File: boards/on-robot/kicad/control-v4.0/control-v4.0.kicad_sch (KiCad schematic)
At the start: 13 parts, among them IC1 MCP23017E_SS, J1 53625-0274, J6 53625-0274, J7 53625-0274, J8 53625-0274, U1 Teensy4.1, U3 NRF24L01_Breakout

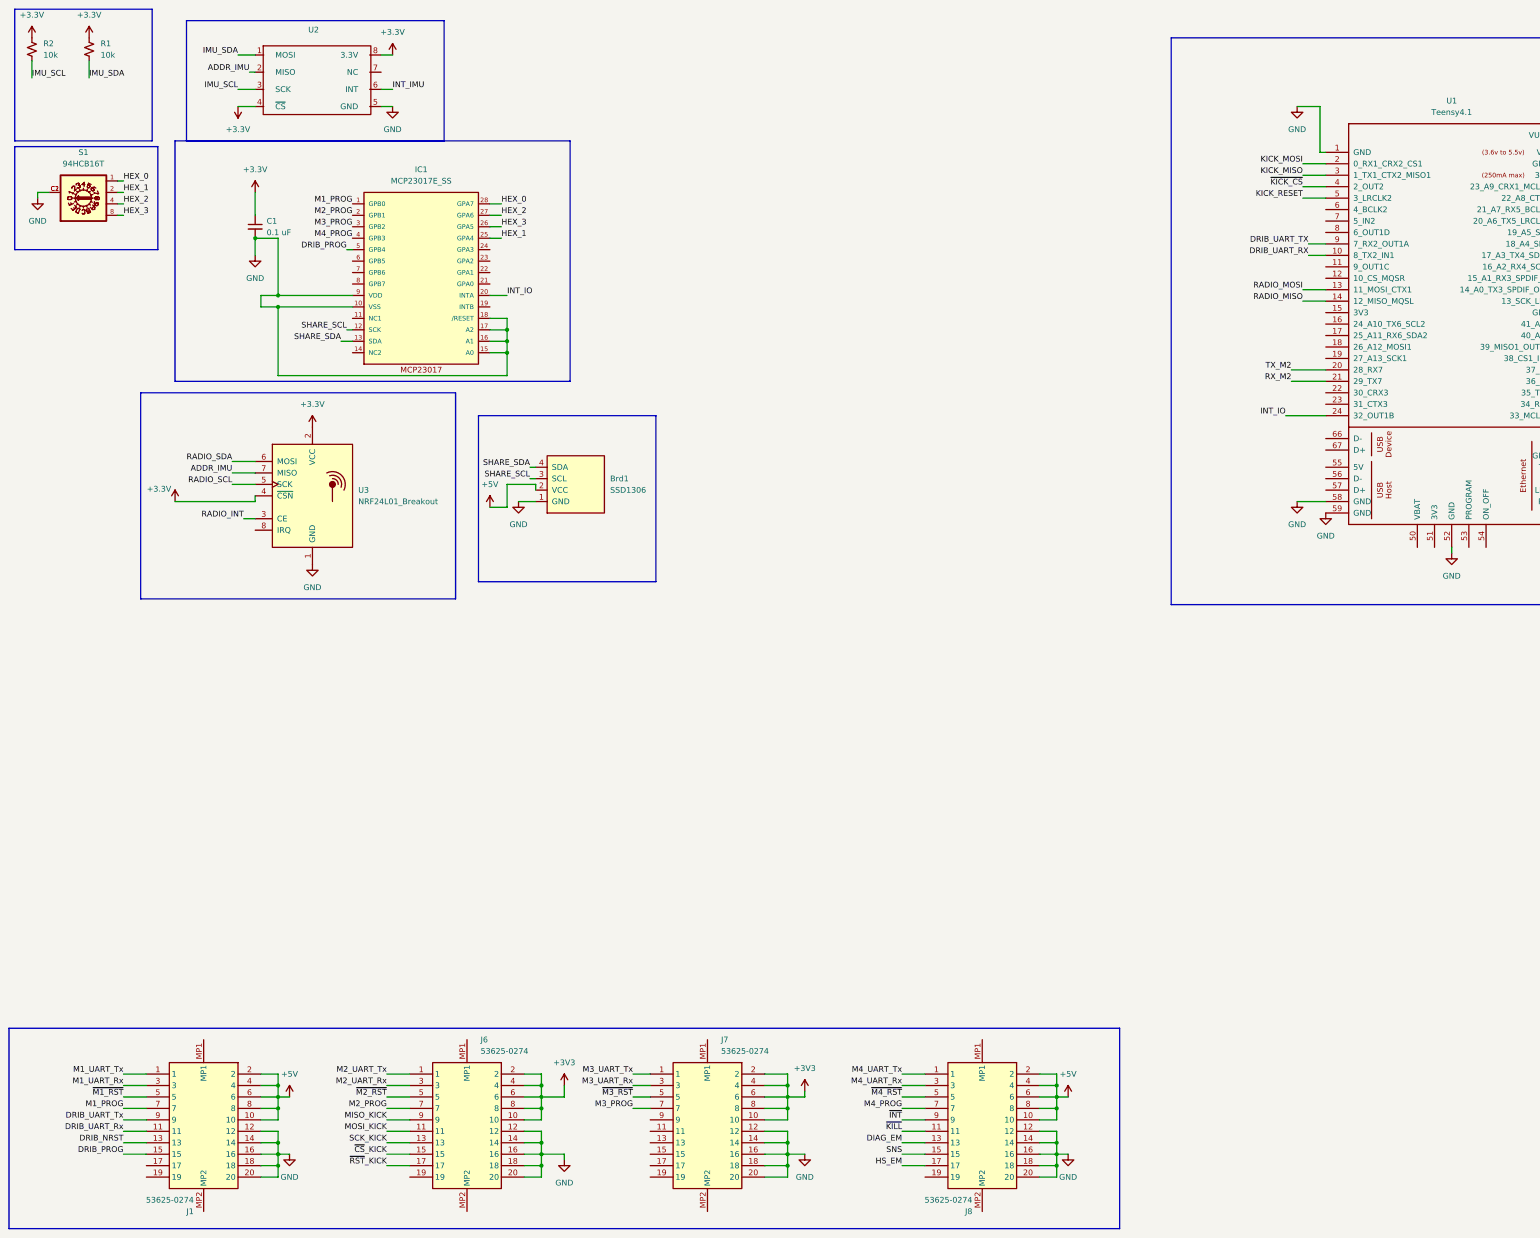
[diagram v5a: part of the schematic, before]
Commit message: migrated libraries
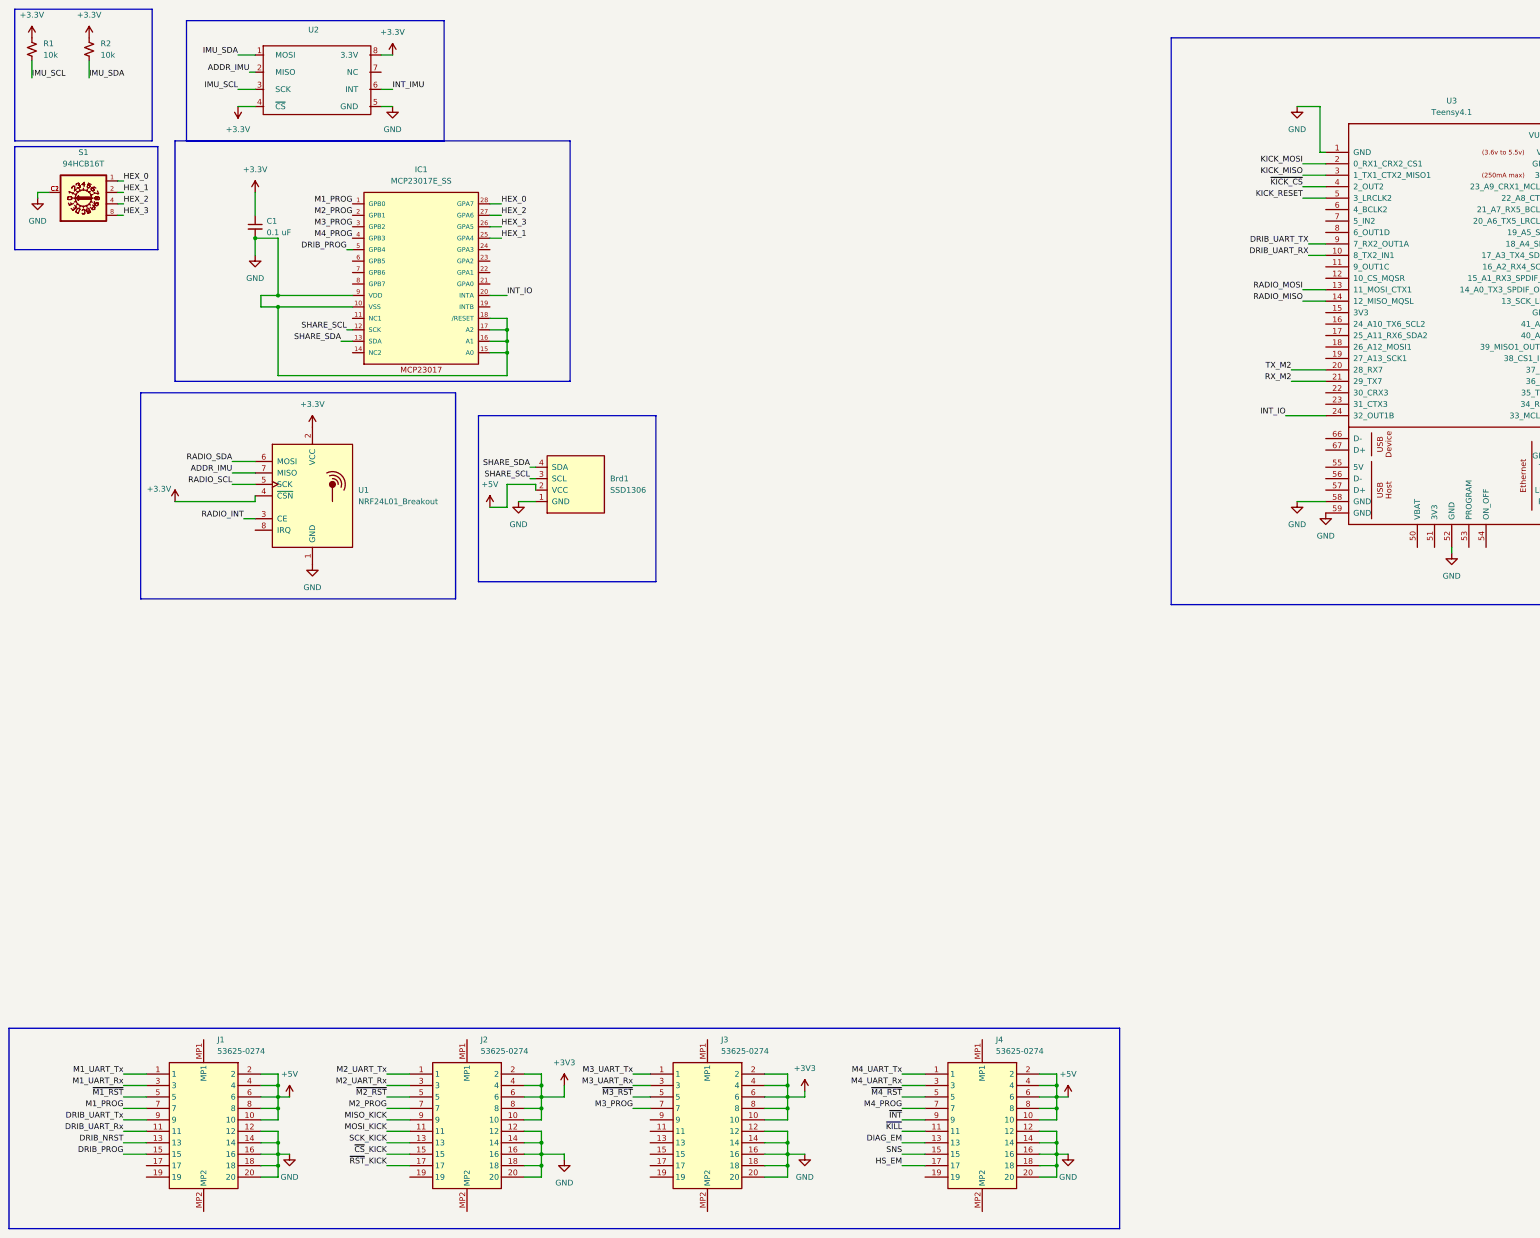
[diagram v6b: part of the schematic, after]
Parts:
- removed J6, J7, J8: 53625-0274, RoboJackets-Connectors:536250274, symbol RoboJackets-Connectors:53625-0274
- added J2, J3, J4: 53625-0274, RoboJackets-Connectors:536250274, symbol RoboJackets-Connectors:53625-0274
- U3: renamed from U1; footprint teensy.pretty-master:Teensy41 -> RoboJackets-Boards:Teensy41
- renumbered R2 to R1, R1 to R2, U3 to U1
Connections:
- net +3V3: now also J2.10, J2.2, J2.4, J2.6, J2.8, J3.10, J3.2, J3.4, J3.6, J3.8
- net +5V: now also J4.10, J4.2, J4.4, J4.6, J4.8
- net DIAG_EM: now also J4.13
- net GND: now also J2.12, J2.14, J2.16, J2.18, J2.20, J3.12, J3.14, J3.16, J3.18, J3.20, J4.12, J4.14, J4.16, J4.18, J4.20
- net HS_EM: now also J4.17
- net M2_PROG: now also J2.7
- net M2_UART_Rx: now also J2.3
- net M2_UART_Tx: now also J2.1
- net M3_PROG: now also J3.7
- net M3_UART_Rx: now also J3.3
- net M3_UART_Tx: now also J3.1
- net M4_PROG: now also J4.7
- net M4_UART_Rx: now also J4.3
- net M4_UART_Tx: now also J4.1
- net MISO_KICK: now also J2.9
- net MOSI_KICK: now also J2.11
- net SCK_KICK: now also J2.13
- net SNS: now also J4.15
- net ~{CS}_KICK: now also J2.15
- net ~{INT}: now also J4.9
- net ~{KILL}: now also J4.11
- net ~{M2_RST}: now also J2.5
- net ~{M3_RST}: now also J3.5
- net ~{M4_RST}: now also J4.5
- net ~{RST}_KICK: now also J2.17

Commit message: design review comments
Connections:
- net GND: no longer IC1.10 (VSS), IC1.15 (A0), IC1.16 (A1), IC1.17 (A2), IC1.18 (/RESET), IC1.9 (VDD)
- new net: IC1.10 (VSS), IC1.15 (A0), IC1.16 (A1), IC1.17 (A2), IC1.18 (/RESET)
- no-connect marks 0 -> 1
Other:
- note added: "CHANGE TEENSY VIN"
- note added: "We have extra pins. Remove IO expander"
- note added: "change this"
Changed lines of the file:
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@@
-	)
-	(junction
-		(at 73.66 78.74)
-		(diameter 0)
-		(color 0 0 0 0)
-	)
-	(junction
-		(at 73.66 76.2)
-		(diameter 0)
-		(color 0 0 0 0)
 	)
 	(junction
@@
 		(color 0 0 0 0)
 	)
+	(no_connect
+		(at 361.95 49.53)
+	)
 	(wire
 		(pts
@@
 	(wire
 		(pts
-			(xy 69.85 78.74) (xy 73.66 78.74)
-		)
-		(stroke
-			(width 0)
-			(type default)
-		)
-	)
-	(wire
-		(pts
 			(xy 361.95 111.76) (xy 368.3 111.76)
 		)
@@
 	(wire
 		(pts
-			(xy 73.66 76.2) (xy 90.17 76.2)
-		)
-		(stroke
-			(width 0)
-			(type default)
-		)
-	)
-	(wire
-		(pts
 			(xy 152.4 254) (xy 156.21 254)
 		)
@@
 	(wire
 		(pts
-			(xy 73.66 76.2) (xy 69.85 76.2)
-		)
-		(stroke
-			(width 0)
-			(type default)
-		)
-	)
-	(wire
-		(pts
 			(xy 246.38 266.7) (xy 248.92 266.7)
 		)
@@
 	(wire
 		(pts
-			(xy 73.66 63.5) (xy 73.66 76.2)
-		)
-		(stroke
-			(width 0)
-			(type default)
-		)
-	)
-	(wire
-		(pts
 			(xy 124.46 93.98) (xy 124.46 88.9)
 		)
@@
 		(pts
 			(xy 124.46 118.11) (xy 130.81 118.11)
-		)
-		(stroke
-			(width 0)
-			(type default)
-		)
-	)
-	(wire
-		(pts
-			(xy 69.85 76.2) (xy 69.85 78.74)
 		)
 		(stroke
@@
 		)
 	)
+	(text "CHANGE TEENSY VIN"
+		(exclude_from_sim no)
+		(at 367.284 36.576 0)
+		(effects
+			(font
+				(size 1.27 1.27)
+				(color 255 0 0 1)
+			)
+		)
+	)
+	(text "change this"
+		(exclude_from_sim no)
+		(at 22.352 63.5 0)
+		(effects
+			(font
+				(size 1.27 1.27)
+				(color 255 0 0 1)
+			)
+		)
+	)
+	(text "We have extra pins.\nRemove IO expander"
+		(exclude_from_sim no)
+		(at 293.116 84.074 0)
+		(effects
+			(font
+				(size 1.27 1.27)
+				(color 255 0 0 1)
+			)
+		)
+	)

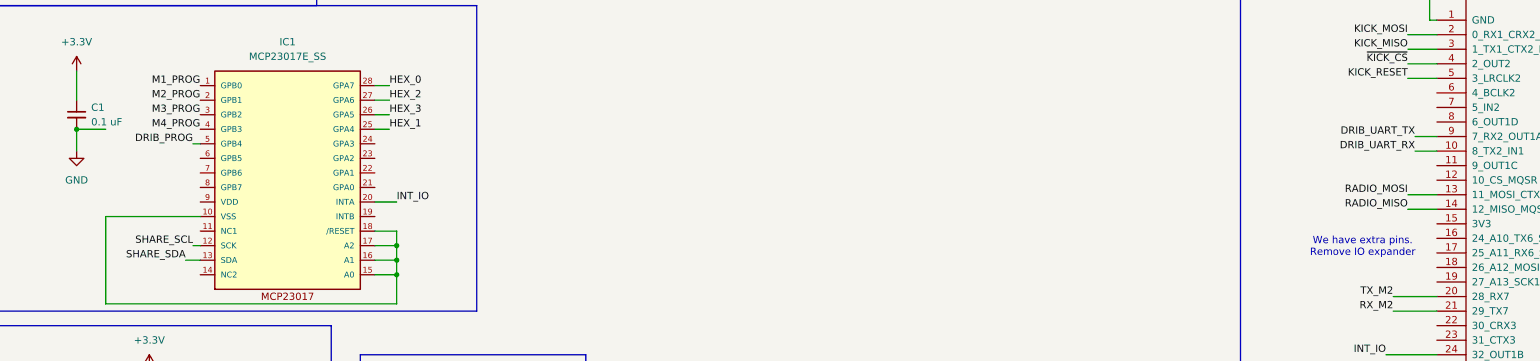
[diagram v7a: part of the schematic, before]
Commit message: fixed MCP23017E_SS wiring? (restored previous version before power label disappeared)
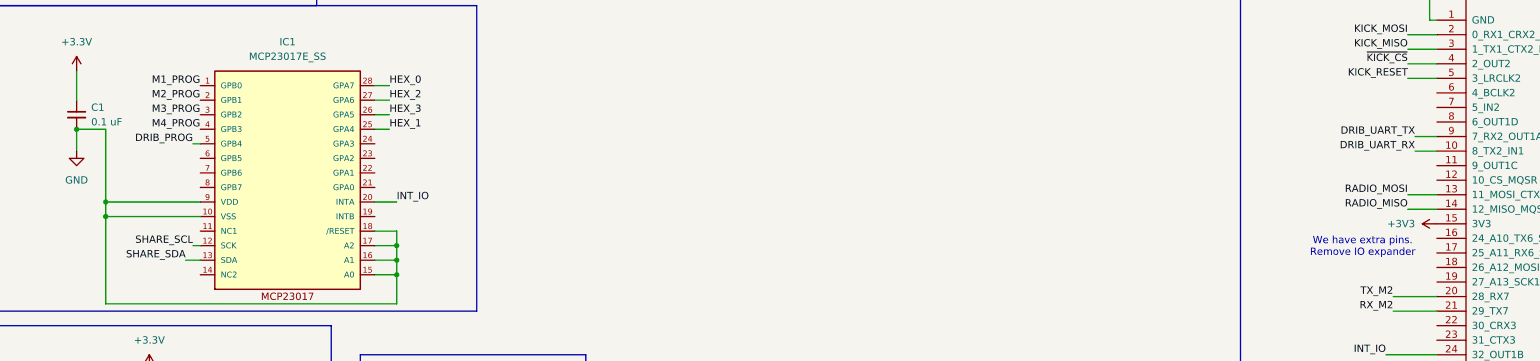
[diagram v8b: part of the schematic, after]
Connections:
- net +3V3: now also U3.15 (3V3)
- net GND: now also IC1.10 (VSS), IC1.15 (A0), IC1.16 (A1), IC1.17 (A2), IC1.18 (/RESET), IC1.9 (VDD)
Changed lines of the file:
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@@
 	)
 	(junction
+		(at 73.66 78.74)
+		(diameter 0)
+		(color 0 0 0 0)
+	)
+	(junction
 		(at 186.69 269.24)
 		(diameter 0)
@@
 		(color 0 0 0 0)
 	)
+	(junction
+		(at 73.66 76.2)
+		(diameter 0)
+		(color 0 0 0 0)
+	)
 	(no_connect
 		(at 361.95 49.53)
@@
 	(wire
 		(pts
+			(xy 73.66 76.2) (xy 90.17 76.2)
+		)
+		(stroke
+			(width 0)
+			(type default)
+		)
+	)
+	(wire
+		(pts
 			(xy 300.99 46.99) (xy 306.07 46.99)
 		)
@@
 	(wire
 		(pts
+			(xy 73.66 76.2) (xy 73.66 78.74)
+		)
+		(stroke
+			(width 0)
+			(type default)
+		)
+	)
+	(wire
+		(pts
 			(xy 132.08 254) (xy 137.16 254)
 		)
@@
 	(wire
 		(pts
+			(xy 73.66 63.5) (xy 73.66 76.2)
+		)
+		(stroke
+			(width 0)
+			(type default)
+		)
+	)
+	(wire
+		(pts
 			(xy 128.27 256.54) (xy 132.08 256.54)
 		)
@@
 		(on_board yes)
 		(dnp no)
-		(fields_autoplaced yes)
 		(property "Reference" "#PWR016"
 			(at 137.16 255.27 0)
@@
 					(unit 1)
 				)
+			)
+		)
+	)
+	(symbol
+		(lib_id "power:+3V3")
+		(at 306.07 80.01 90)
+		(unit 1)
+		(exclude_from_sim no)
+		(in_bom yes)
+		(on_board yes)
+		(dnp no)
+		(fields_autoplaced yes)
+		(property "Reference" "#PWR031"
+			(at 309.88 80.01 0)
+			(effects
+				(font
+					(size 1.27 1.27)
+				)
+				(hide yes)
+			)
+		)
+		(property "Value" "+3V3"
+			(at 302.26 80.0099 90)
+			(effects
+				(font
+					(size 1.27 1.27)
+				)
+				(justify left)
+			)
+		)
+		(property "Footprint" ""
+			(at 306.07 80.01 0)
+			(effects
+				(font
+					(size 1.27 1.27)
+				)
+				(hide yes)
+			)
+		)
+		(property "Datasheet" ""
+			(at 306.07 80.01 0)
+			(effects
+				(font
+					(size 1.27 1.27)
+				)
+				(hide yes)
+			)
+		)
+		(property "Description" "Power symbol creates a global label with name \"+3V3\""
+			(at 306.07 80.01 0)
+			(effects
+				(font
+					(size 1.27 1.27)
+				)
+				(hide yes)
+			)
+		)
+		(pin "1"
+		)
+		(instances
+			(project ""
+				(path "/ae565616-1e9e-4753-8357-99638ad3b9f6"
+					(reference "#PWR031")
+					(unit 1)
+				)
